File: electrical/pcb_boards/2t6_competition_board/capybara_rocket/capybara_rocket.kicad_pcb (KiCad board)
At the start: 2 copper layers, 130 x 60 mm, 1 part, among them U1 WRL-11812

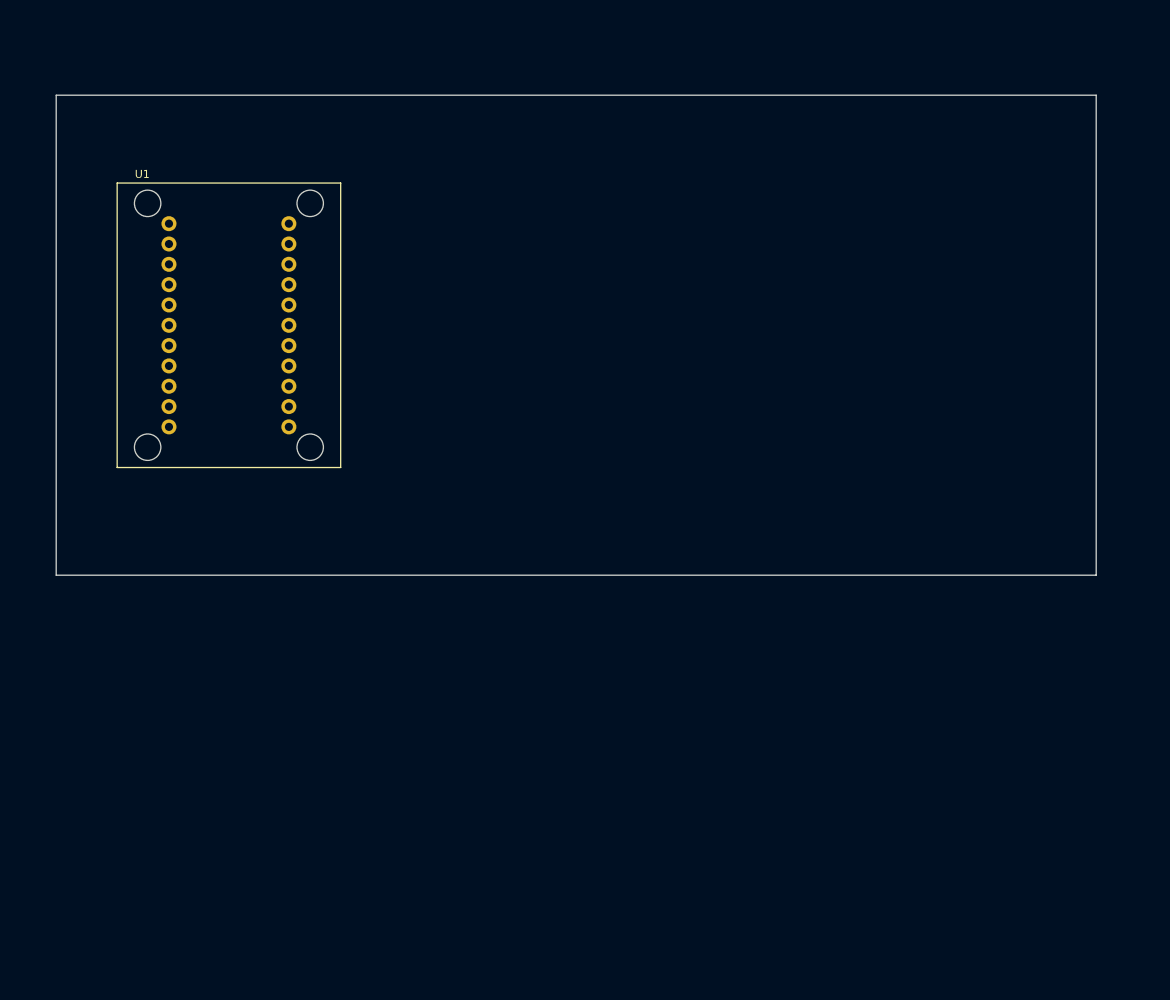
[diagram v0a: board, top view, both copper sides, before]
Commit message: Adding new KiCad symbols and footprints and initial PCB dimension work
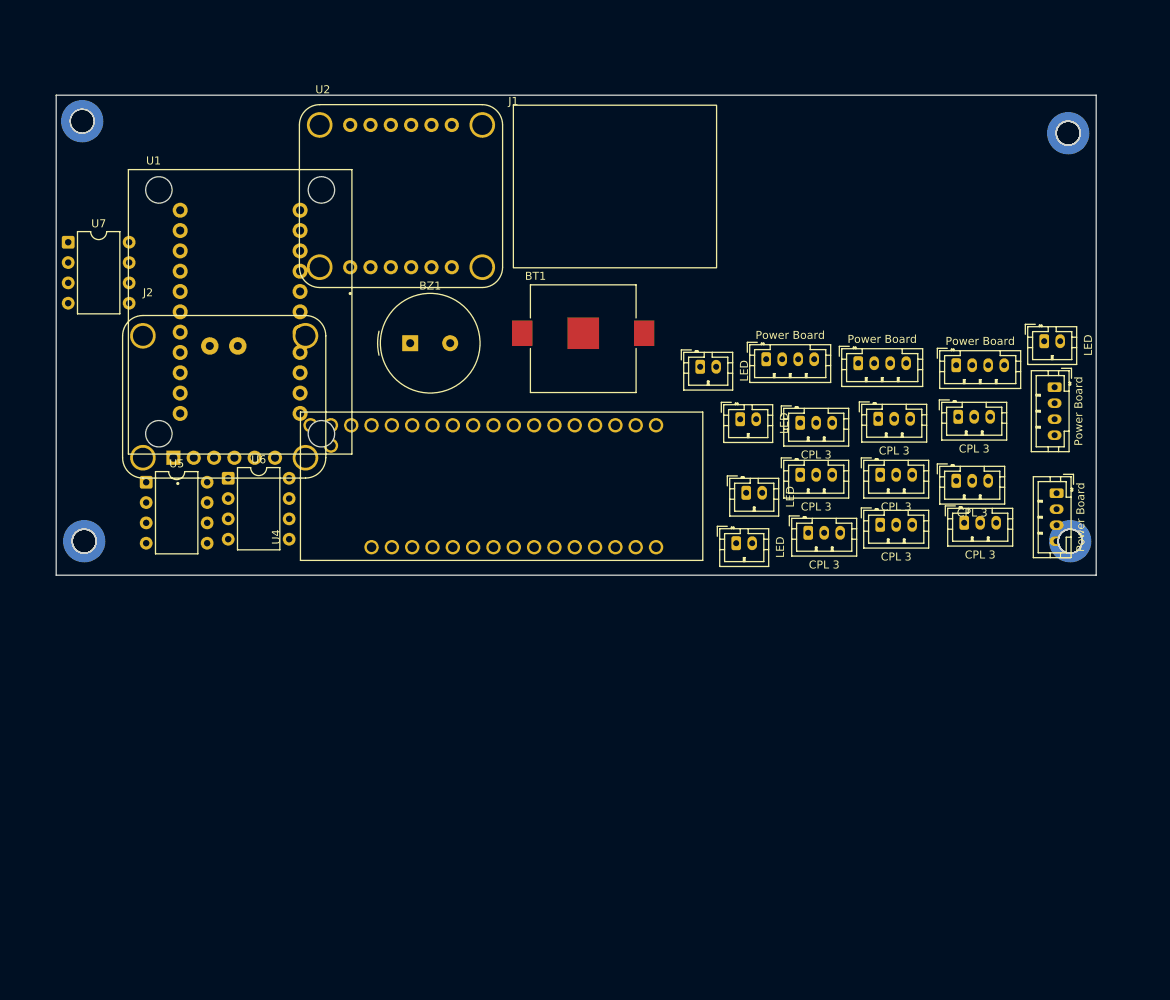
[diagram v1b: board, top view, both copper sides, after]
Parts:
- added ? (x3): , , F.Cu at (88.5, 125.8)
- added ? (x3): , , F.Cu at (211.8, 125.8)
- added ?: , , F.Cu at (88.2, 73.2)
- added ? (x3): , , F.Cu at (211.5, 74.8)
- added BT1: 2894TR, RSX_CanSat_Custom_KiCad_Footprints:BAT_2894TR, F.Cu at (150.9, 99.8)
- added BZ1: Buzzer, Buzzer_Beeper:Buzzer_TDK_PS1240P02BT_D12.2mm_H6.5mm, F.Cu at (129.2, 101.0)
- added J1: Power Board, Connector_JST:JST_PH_B4B-PH-K_1x04_P2.00mm_Vertical, F.Cu at (173.8, 103.0)
- added J1: Conn_01x08_Pin, RSX_CanSat_Custom_KiCad_Footprints:Adafruit_BMP581, F.Cu at (142.1, 71.3)
- added J1: Power Board, Connector_JST:JST_PH_B4B-PH-K_1x04_P2.00mm_Vertical, F.Cu at (197.5, 103.8)
- added J1: Power Board, Connector_JST:JST_PH_B4B-PH-K_1x04_P2.00mm_Vertical, F.Cu at (185.2, 103.5)
- added J1: Power Board, Connector_JST:JST_PH_B4B-PH-K_1x04_P2.00mm_Vertical, F.Cu at (210.1, 119.8)
- added J1: Power Board, Connector_JST:JST_PH_B4B-PH-K_1x04_P2.00mm_Vertical, F.Cu at (209.8, 106.5)
- added J11: CPL 3, Connector_JST:JST_PH_B3B-PH-K_1x03_P2.00mm_Vertical, F.Cu at (198.5, 123.5)
- added J11: CPL 3, Connector_JST:JST_PH_B3B-PH-K_1x03_P2.00mm_Vertical, F.Cu at (187.8, 110.5)
- added J11: CPL 3, Connector_JST:JST_PH_B3B-PH-K_1x03_P2.00mm_Vertical, F.Cu at (179.0, 124.7)
- added J11: CPL 3, Connector_JST:JST_PH_B3B-PH-K_1x03_P2.00mm_Vertical, F.Cu at (197.5, 118.2)
- added J11: CPL 3, Connector_JST:JST_PH_B3B-PH-K_1x03_P2.00mm_Vertical, F.Cu at (188.0, 117.5)
- added J11: CPL 3, Connector_JST:JST_PH_B3B-PH-K_1x03_P2.00mm_Vertical, F.Cu at (178.0, 111.0)
- added J11: CPL 3, Connector_JST:JST_PH_B3B-PH-K_1x03_P2.00mm_Vertical, F.Cu at (197.8, 110.2)
- added J11: CPL 3, Connector_JST:JST_PH_B3B-PH-K_1x03_P2.00mm_Vertical, F.Cu at (188.0, 123.7)
- added J11: CPL 3, Connector_JST:JST_PH_B3B-PH-K_1x03_P2.00mm_Vertical, F.Cu at (178.0, 117.5)
- added J2: Conn_01x06_Pin, RSX_CanSat_Custom_KiCad_Footprints:MODULE_904, F.Cu at (93.3, 117.9)
- added J5: LED, Connector_JST:JST_PH_B2B-PH-K_1x02_P2.00mm_Vertical, F.Cu at (208.5, 100.8)
- added J5: LED, Connector_JST:JST_PH_B2B-PH-K_1x02_P2.00mm_Vertical, F.Cu at (170.0, 126.0)
- added J5: LED, Connector_JST:JST_PH_B2B-PH-K_1x02_P2.00mm_Vertical, F.Cu at (171.2, 119.7)
- added J5: LED, Connector_JST:JST_PH_B2B-PH-K_1x02_P2.00mm_Vertical, F.Cu at (165.5, 104.0)
- added J5: LED, Connector_JST:JST_PH_B2B-PH-K_1x02_P2.00mm_Vertical, F.Cu at (170.5, 110.5)
- added REF**: WA-SMSI_9774030243, DigiKey:WA-SMSI_9774030243, B.Cu at (88.2, 73.2)
- added REF**: WA-SMSI_9774030243, DigiKey:WA-SMSI_9774030243, B.Cu at (211.5, 74.8)
- added REF**: WA-SMSI_9774030243, DigiKey:WA-SMSI_9774030243, B.Cu at (88.5, 125.8)
- added REF**: WA-SMSI_9774030243, DigiKey:WA-SMSI_9774030243, B.Cu at (211.8, 125.8)
- added U2: 4754, RSX_CanSat_Custom_KiCad_Footprints:MODULE_4754, F.Cu at (128.1, 82.6)
- added U4: NUCLEO-G431KB, RSX_CanSat_Custom_KiCad_Footprints:MODULE_NUCLEO-G431KB, F.Cu at (140.7, 118.9)
- added U5: DS1307+, Package_DIP:DIP-8_W7.62mm, F.Cu at (96.2, 118.4)
- added U6: DS1307+, Package_DIP:DIP-8_W7.62mm, F.Cu at (106.5, 117.9)
- added U7: DS1307+, Package_DIP:DIP-8_W7.62mm, F.Cu at (86.5, 88.4)
- moved U1 2.19 mm to (108.0, 97.1)

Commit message: pcb board update w/ new symbols, footprints, and 3dmodels
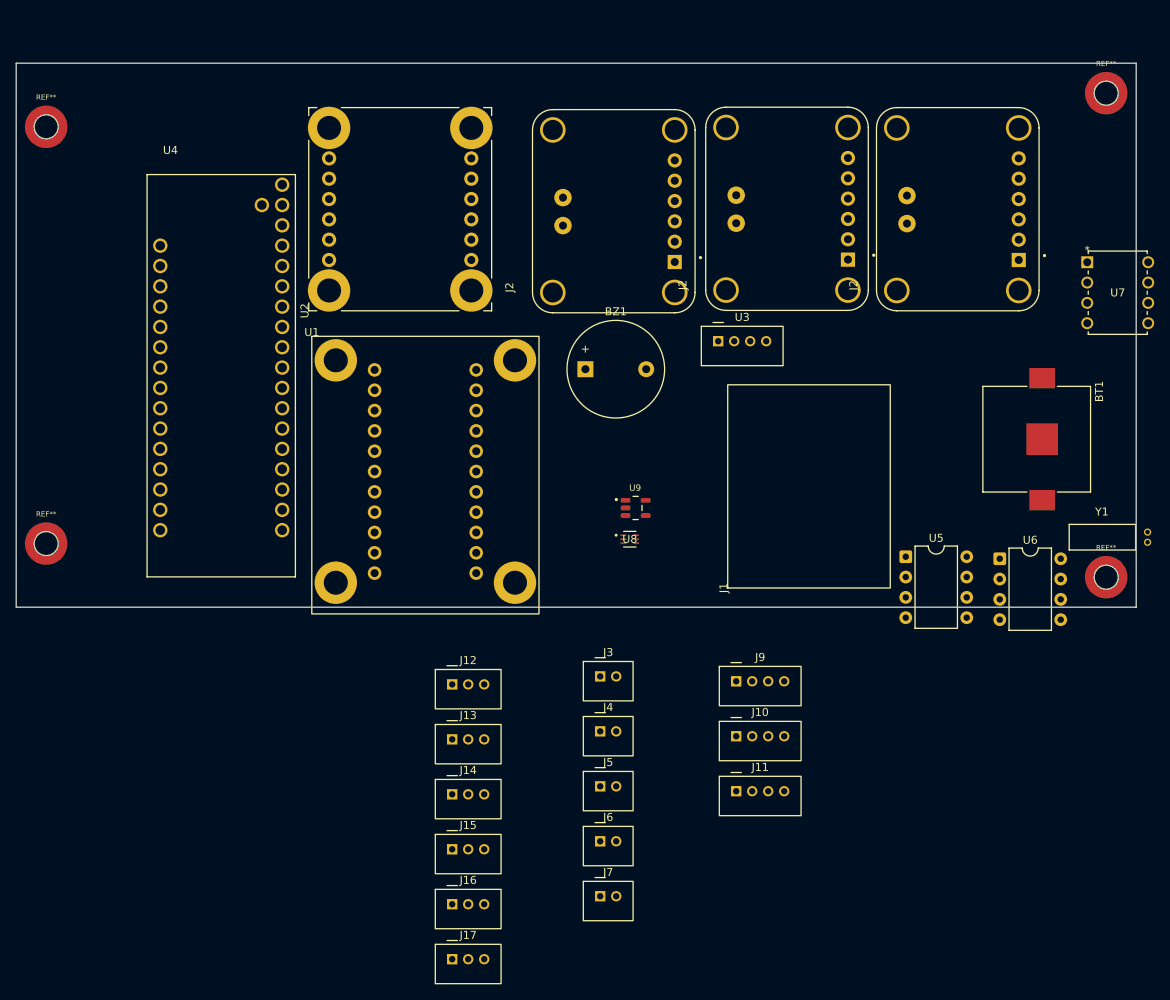
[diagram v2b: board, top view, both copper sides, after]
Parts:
- removed ? (x10): , 
- removed the J1 at (173.8, 103.0)
- removed the J1 at (197.5, 103.8)
- removed the J1 at (185.2, 103.5)
- removed the J1 at (210.1, 119.8)
- removed the J1 at (209.8, 106.5)
- removed the J11 at (198.5, 123.5)
- removed the J11 at (187.8, 110.5)
- removed the J11 at (179.0, 124.7)
- removed the J11 at (197.5, 118.2)
- removed the J11 at (188.0, 117.5)
- removed the J11 at (178.0, 111.0)
- removed the J11 at (197.8, 110.2)
- removed the J11 at (188.0, 123.7)
- removed the J11 at (178.0, 117.5)
- removed the J5 at (208.5, 100.8)
- removed the J5 at (170.0, 126.0)
- removed the J5 at (171.2, 119.7)
- removed the J5 at (165.5, 104.0)
- removed the J5 at (170.5, 110.5)
- removed the REF** at (88.2, 73.2)
- removed the REF** at (211.5, 74.8)
- removed the REF** at (88.5, 125.8)
- removed the REF** at (211.8, 125.8)
- added J10: Wurth_M4_62000411622, RSX_CanSat_Custom_KiCad_Footprints:J_Wurth_WR-WTB_62000411622, F.Cu at (170.0, 150.1)
- added J11: Wurth_M4_62000411622, RSX_CanSat_Custom_KiCad_Footprints:J_Wurth_WR-WTB_62000411622, F.Cu at (170.0, 157.0)
- added J12: Wurth_M3_62000311622, RSX_CanSat_Custom_KiCad_Footprints:J_Wurth_WR-WTB_62000311622, F.Cu at (134.5, 143.7)
- added J13: Wurth_M3_62000311622, RSX_CanSat_Custom_KiCad_Footprints:J_Wurth_WR-WTB_62000311622, F.Cu at (134.5, 150.5)
- added J14: Wurth_M3_62000311622, RSX_CanSat_Custom_KiCad_Footprints:J_Wurth_WR-WTB_62000311622, F.Cu at (134.5, 157.4)
- added J15: Wurth_M3_62000311622, RSX_CanSat_Custom_KiCad_Footprints:J_Wurth_WR-WTB_62000311622, F.Cu at (134.5, 164.3)
- added J16: Wurth_M3_62000311622, RSX_CanSat_Custom_KiCad_Footprints:J_Wurth_WR-WTB_62000311622, F.Cu at (134.5, 171.1)
- added J17: Wurth_M3_62000311622, RSX_CanSat_Custom_KiCad_Footprints:J_Wurth_WR-WTB_62000311622, F.Cu at (134.5, 178.0)
- added J2: Conn_01x06_Pin, RSX_CanSat_Custom_KiCad_Footprints:MODULE_904, F.Cu at (207.9, 97.0)
- added J2: Conn_01x06_Pin, RSX_CanSat_Custom_KiCad_Footprints:MODULE_904, F.Cu at (186.5, 96.9)
- added J3: Wurth_M2_62000211622, RSX_CanSat_Custom_KiCad_Footprints:J_Wurth_WR-WTB_62000211622, F.Cu at (153.0, 142.7)
- added J4: Wurth_M2_62000211622, RSX_CanSat_Custom_KiCad_Footprints:J_Wurth_WR-WTB_62000211622, F.Cu at (153.0, 149.5)
- added J5: Wurth_M2_62000211622, RSX_CanSat_Custom_KiCad_Footprints:J_Wurth_WR-WTB_62000211622, F.Cu at (153.0, 156.4)
- added J6: Wurth_M2_62000211622, RSX_CanSat_Custom_KiCad_Footprints:J_Wurth_WR-WTB_62000211622, F.Cu at (153.0, 163.3)
- added J7: Wurth_M2_62000211622, RSX_CanSat_Custom_KiCad_Footprints:J_Wurth_WR-WTB_62000211622, F.Cu at (153.0, 170.1)
- added J9: Wurth_M4_62000411622, RSX_CanSat_Custom_KiCad_Footprints:J_Wurth_WR-WTB_62000411622, F.Cu at (170.0, 143.3)
- added REF**: WA-SMSI_9774030243, RSX_CanSat_Custom_KiCad_Footprints:WA-SMSI_9774030243, F.Cu at (216.2, 130.2)
- added REF**: WA-SMSI_9774030243, RSX_CanSat_Custom_KiCad_Footprints:WA-SMSI_9774030243, F.Cu at (83.8, 74.0)
- added REF**: WA-SMSI_9774030243, RSX_CanSat_Custom_KiCad_Footprints:WA-SMSI_9774030243, F.Cu at (216.2, 69.8)
- added REF**: WA-SMSI_9774030243, RSX_CanSat_Custom_KiCad_Footprints:WA-SMSI_9774030243, F.Cu at (83.8, 126.0)
- added U3: VL53L1-SATEL, RSX_CanSat_Custom_KiCad_Footprints:J_Wurth_WR-WTB_62000411622, F.Cu at (167.8, 100.8)
- added U8: DRV8212DRLR, RSX_CanSat_Custom_KiCad_Footprints:SOT6_DRV8212_TEX, F.Cu at (156.7, 125.5)
- added U9: SN74LVC1G04DBVR, RSX_CanSat_Custom_KiCad_Footprints:SOT95P280X145-5N, F.Cu at (157.4, 121.6)
- added Y1: AB38T-32.768KHZ, RSX_CanSat_Custom_KiCad_Footprints:XTAL_AB38T-32.768KHZ, F.Cu at (221.4, 125.2)
- BZ1: footprint Buzzer_Beeper:Buzzer_TDK_PS1240P02BT_D12.2mm_H6.5mm -> Buzzer_Beeper:Buzzer_12x9.5RM7.6
- U1: footprint RSX_CanSat_Custom_KiCad_Footprints:MODULE_WRL-11812 -> RSX_CanSat_Custom_KiCad_Footprints:SparkFun_XBee_Explorer_Regulated
- U2: footprint RSX_CanSat_Custom_KiCad_Footprints:MODULE_4754 -> RSX_CanSat_Custom_KiCad_Footprints:Adafruit_BNO085
- U6: value DS1307+ -> NE555P
- U7: value DS1307+ -> 25LC1024-E/P; footprint Package_DIP:DIP-8_W7.62mm -> RSX_CanSat_Custom_KiCad_Footprints:PDIP8_300MC_MCH
- moved U7 127.4 mm to (213.9, 90.9)
- moved U6 97.0 mm to (202.9, 127.9)
- moved U5 95.4 mm to (191.2, 127.7)
- moved J2 74.5 mm to (164.9, 97.2), turned to 90 degrees
- moved J1 66.0 mm to (168.9, 131.6), turned to 90 degrees
- moved BT1 58.9 mm to (208.2, 113.0), turned to -90 degrees
- moved U4 37.7 mm to (105.6, 105.1), turned to 0 degrees
- moved BZ1 22.1 mm to (151.2, 104.2)
- moved U2 18.4 mm to (116.6, 97.0), turned to 90 degrees
- moved U1 9.47 mm to (117.0, 100.1)
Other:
- board size 130 x 60 mm -> 140 x 68 mm
- copper layers 2 -> 4

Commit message: Adding buck boost components
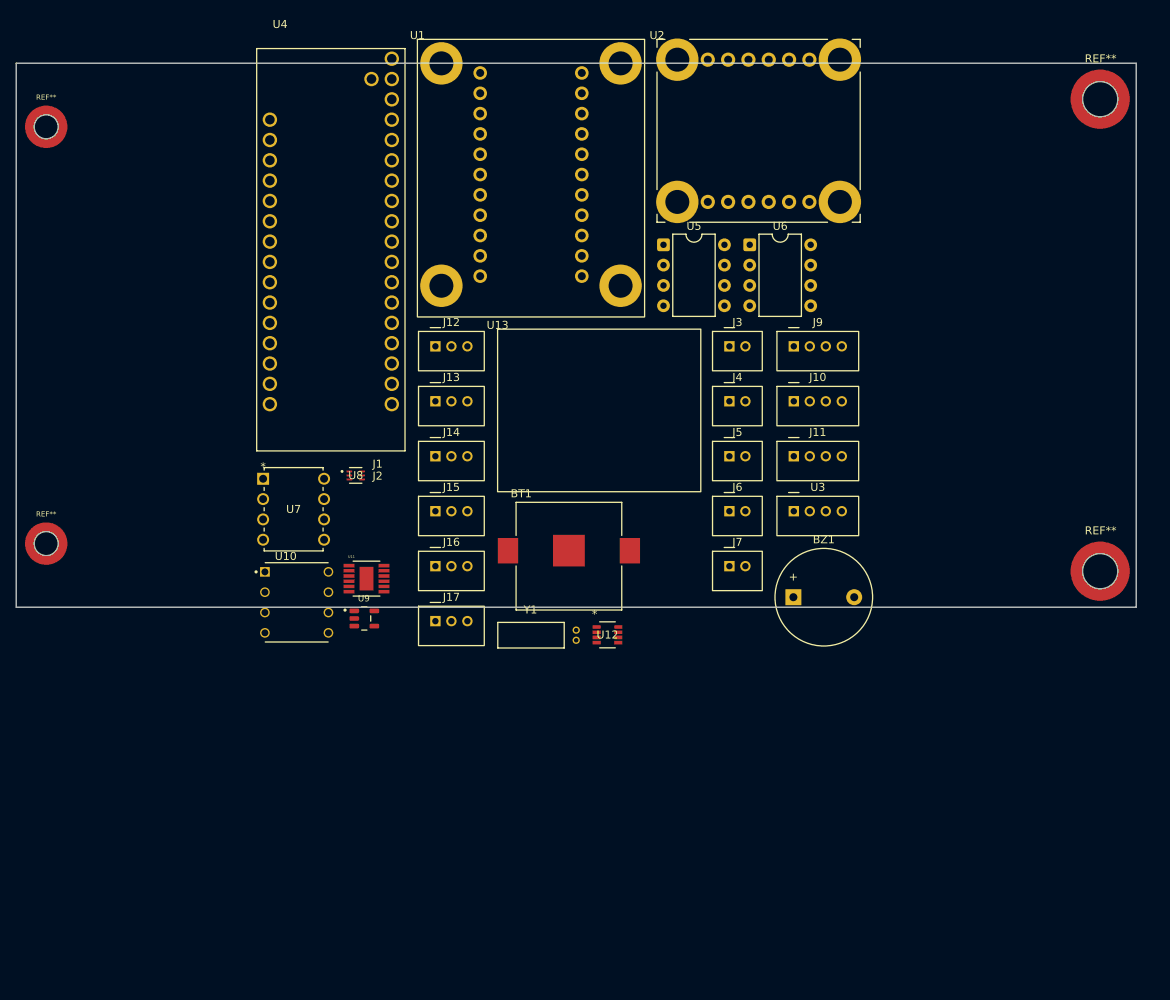
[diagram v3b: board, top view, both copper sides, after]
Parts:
- removed the J2 at (207.9, 97.0)
- removed the J2 at (164.9, 97.2)
- removed the J2 at (186.5, 96.9)
- removed the REF** at (216.2, 130.2)
- removed the REF** at (216.2, 69.8)
- added J2: Conn_01x06_Pin, RSX_CanSat_Custom_KiCad_Footprints:Adafruit_INA219, F.Cu at (125.2, 118.1)
- added REF**: WA-SMSI_9774030360, RSX_CanSat_Custom_KiCad_Footprints:WA-SMSI_9774030360, F.Cu at (215.5, 129.5)
- added REF**: WA-SMSI_9774030360, RSX_CanSat_Custom_KiCad_Footprints:WA-SMSI_9774030360, F.Cu at (215.5, 70.5)
- added U10: MAX756CPA_, RSX_CanSat_Custom_KiCad_Footprints:DIP794W47P254L991H457Q8, F.Cu at (115.1, 133.4)
- added U11: LTC3536EMSE_PBF, RSX_CanSat_Custom_KiCad_Footprints:MSOP-12_MSE, F.Cu at (123.8, 130.4)
- added U12: MP3414AGJ-Z, RSX_CanSat_Custom_KiCad_Footprints:TSOT23-8_MP3414A, F.Cu at (153.9, 137.5)
- added U13: Adafruit_BMP581, RSX_CanSat_Custom_KiCad_Footprints:Adafruit_BMP581, F.Cu at (140.2, 99.2)
- J1: value Conn_01x08_Pin -> Wurth_M4_62000411622; footprint RSX_CanSat_Custom_KiCad_Footprints:Adafruit_BMP581 -> RSX_CanSat_Custom_KiCad_Footprints:SparkFun_GNSS_MAX_M10S
- moved U7 106.5 mm to (110.9, 117.9)
- moved Y1 72.5 mm to (150.0, 137.5)
- moved BT1 60.8 mm to (149.1, 126.9), turned to 0 degrees
- moved U2 55.2 mm to (160.1, 63.0), turned to 0 degrees
- moved U6 50.2 mm to (171.7, 88.7)
- moved U5 49.4 mm to (160.9, 88.7)
- moved J1 46.3 mm to (125.2, 116.6), turned to 0 degrees
- moved J3 44.3 mm to (169.2, 101.4)
- moved J4 44.3 mm to (169.2, 108.3)
- moved J5 44.3 mm to (169.2, 115.1)
- moved J6 44.3 mm to (169.2, 122.0)
- moved J7 44.3 mm to (169.2, 128.9)
- moved J11 42.5 mm to (177.2, 115.1)
- moved J10 42.5 mm to (177.2, 108.3)
- moved J9 42.5 mm to (177.2, 101.4)
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
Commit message: PCB board arrangement update and Adafruit INA219 full footprint design
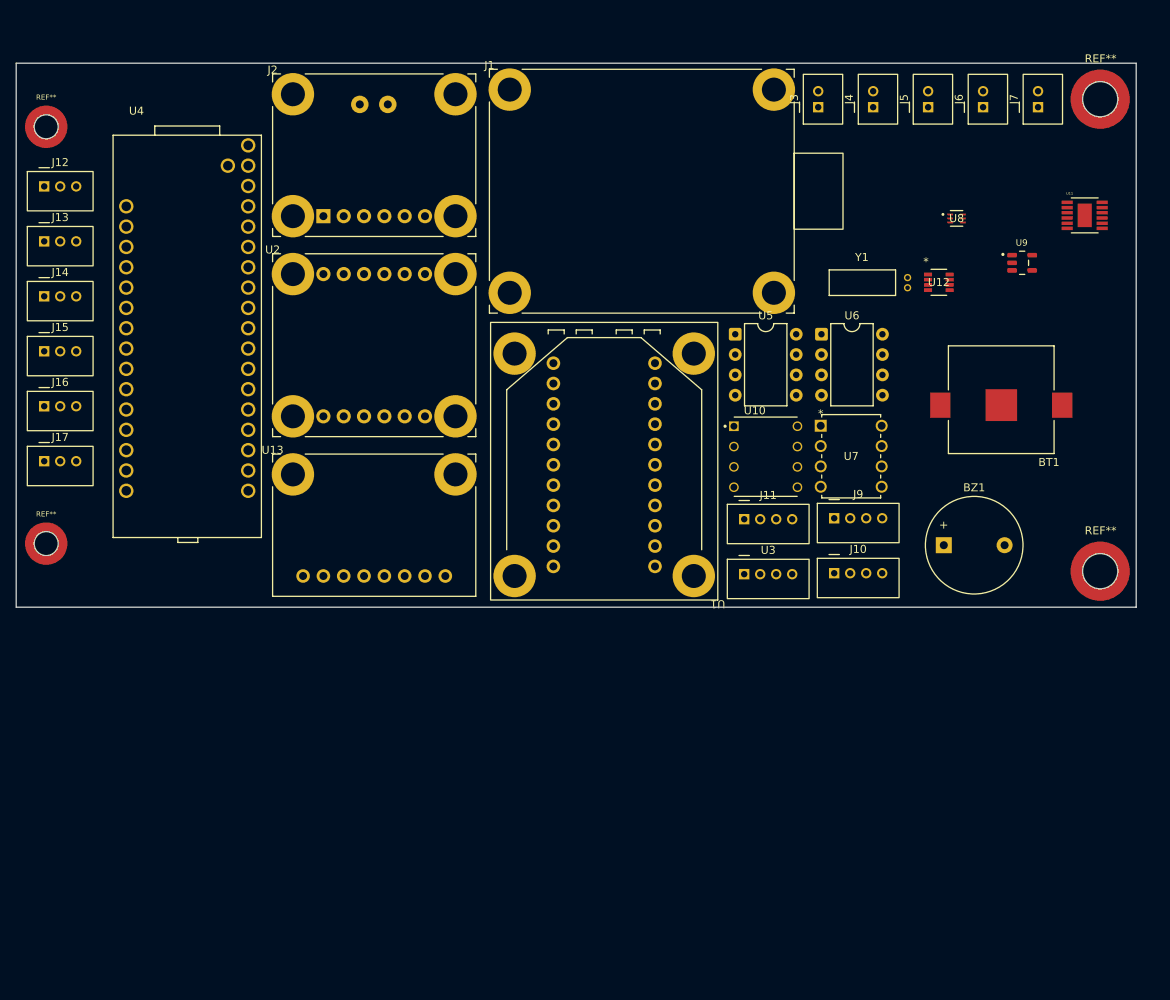
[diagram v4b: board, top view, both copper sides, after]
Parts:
- moved U11 100.6 mm to (213.6, 85.0)
- moved U9 93.5 mm to (205.7, 91.0)
- moved U8 81.7 mm to (197.6, 85.4)
- moved U1 79.5 mm to (167.7, 133.1), turned to 180 degrees
- moved U7 70.0 mm to (180.6, 111.3)
- moved J7 69.1 mm to (207.7, 71.5), turned to 90 degrees
- moved U10 61.4 mm to (173.7, 115.2)
- moved Y1 60.5 mm to (191.4, 93.4)
- moved U12 60.5 mm to (195.3, 93.4)
- moved J6 59.6 mm to (200.9, 71.5), turned to 90 degrees
- moved BT1 57.0 mm to (203.1, 108.8), turned to 180 degrees
- moved U2 55.0 mm to (112.0, 89.8)
- moved J13 52.8 mm to (83.5, 88.3)
- moved J16 52.8 mm to (83.5, 108.9)
- moved J17 52.8 mm to (83.5, 115.8)
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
